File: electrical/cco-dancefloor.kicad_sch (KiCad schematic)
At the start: 3 parts, among them J1 Conn_01x04_Pin, U1 ESP32-S3, U2 A1101xLH

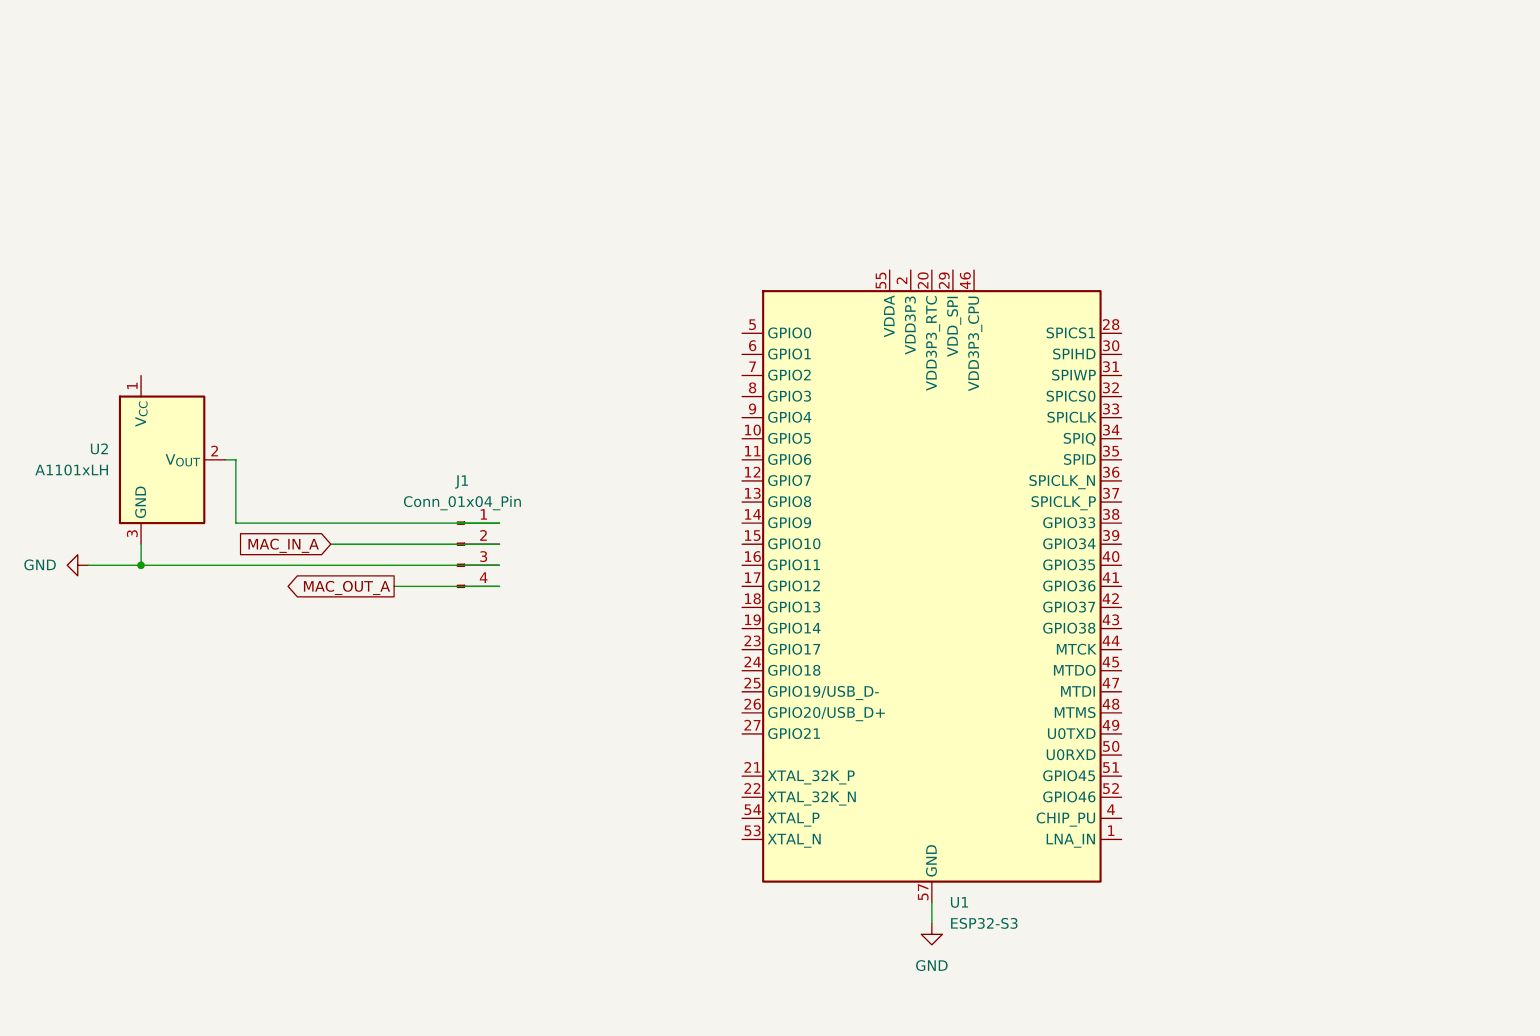
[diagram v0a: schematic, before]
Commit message: muxes and mcu || todo: clean up discarded files and improve documentation
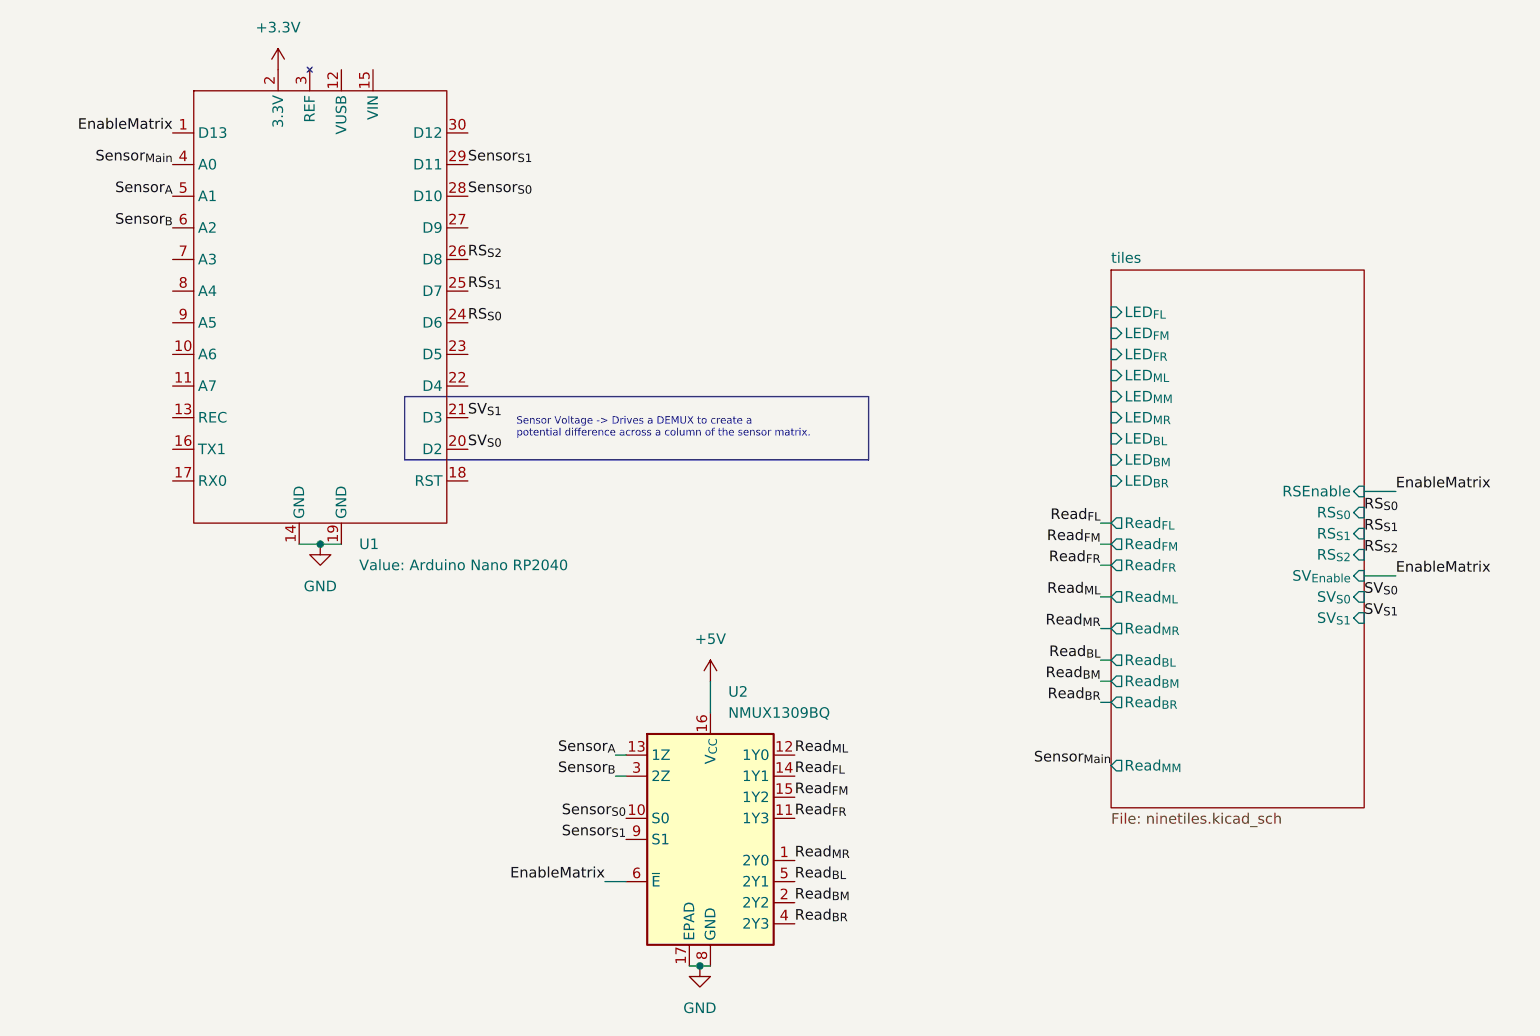
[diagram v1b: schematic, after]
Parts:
- removed J1: Conn_01x04_Pin, symbol Connector:Conn_01x04_Pin
- removed U1: ESP32-S3, Package_DFN_QFN:QFN-56-1EP_7x7mm_P0.4mm_EP4x4mm, symbol MCU_Espressif:ESP32-S3
- removed U2: A1101xLH, Package_TO_SOT_SMD:SOT-23W, symbol Sensor_Magnetic:A1101xLH
- added U1: Arduino Nano RP2040, symbol kenny:arduino_rp2040
- added U2: NMUX1309BQ, Package_DFN_QFN:DHVQFN-16-1EP_2.5x3.5mm_P0.5mm_EP1x2mm, symbol Analog_Switch:NMUX1309BQ
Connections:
- net GND: now also U1.14 (GND), U1.19 (GND), U2.17 (EPAD), U2.8 (GND)
- new net +3.3V: U1.2 (3.3V)
- new net +5V: U2.16 (V_{CC})
- new net EnableMatrix: U1.1 (D13), U2.6 (~{E})
- new net RS_{S0}: U1.24 (D6)
- new net RS_{S1}: U1.25 (D7)
- new net RS_{S2}: U1.26 (D8)
- new net Read_{BL}: U2.5 (2Y1)
- new net Read_{BM}: U2.2 (2Y2)
- new net Read_{BR}: U2.4 (2Y3)
- new net Read_{FL}: U2.14 (1Y1)
- new net Read_{FM}: U2.15 (1Y2)
- new net Read_{FR}: U2.11 (1Y3)
- new net Read_{ML}: U2.12 (1Y0)
- new net Read_{MR}: U2.1 (2Y0)
- new net SV_{S0}: U1.20 (D2)
- new net SV_{S1}: U1.21 (D3)
- new net Sensor_{A}: U1.5 (A1), U2.13 (1Z)
- new net Sensor_{B}: U1.6 (A2), U2.3 (2Z)
- new net Sensor_{Main}: U1.4 (A0)
- new net Sensor_{S0}: U1.28 (D10), U2.10 (S0)
- new net Sensor_{S1}: U1.29 (D11), U2.9 (S1)
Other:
- added sheet tiles (ninetiles.kicad_sch)
- note added: "Sensor Voltage -> Drives a DEMUX to create a potential difference across a column of the sensor matrix."
